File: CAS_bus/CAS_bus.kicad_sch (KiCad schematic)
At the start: 1 part, among them J5 CAS_stacking

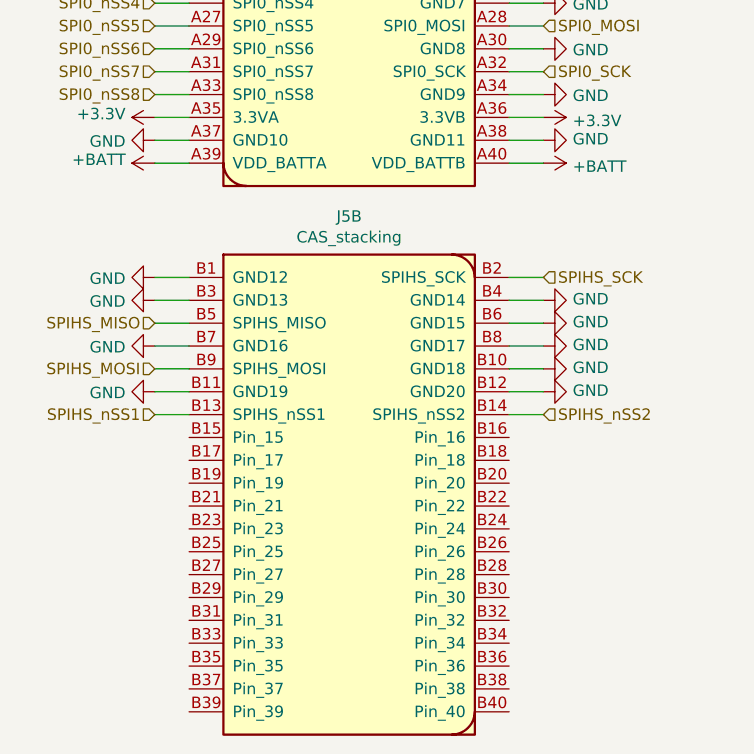
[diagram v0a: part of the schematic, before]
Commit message: Updated-cas-bus-sch
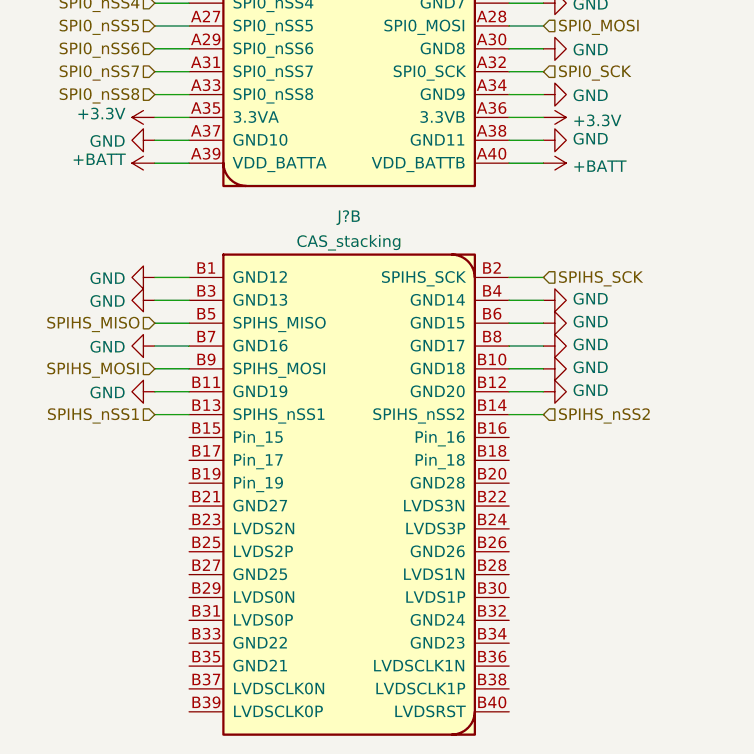
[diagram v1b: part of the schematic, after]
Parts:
- removed unit 2 of J5
- added J?: CAS_stacking, symbol star-common-lib:CAS_stacking
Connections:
- net GND: now also J?.B1 (GND12), J?.B10 (GND18), J?.B11 (GND19), J?.B12 (GND20), J?.B3 (GND13), J?.B4 (GND14), J?.B6 (GND15), J?.B7 (GND16), J?.B8 (GND17)
- net SPIHS_MISO: now also J?.B5 (SPIHS_MISO)
- net SPIHS_MOSI: now also J?.B9 (SPIHS_MOSI)
- net SPIHS_SCK: now also J?.B2 (SPIHS_SCK)
- net SPIHS_nSS1: now also J?.B13 (SPIHS_nSS1)
- net SPIHS_nSS2: now also J?.B14 (SPIHS_nSS2)
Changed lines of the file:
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@@
     (pin "1")
+  )
+  (symbol (lib_name "CAS_stacking_1") (lib_id "star-common-lib:CAS_stacking") (at 130.81 130.81 0) (unit 2)
+    (in_bom yes) (on_board yes) (fields_autoplaced)
+    (property "Reference" "J?" (id 0) (at 130.81 99.9195 0))
+    (property "Value" "CAS_stacking" (id 1) (at 130.81 102.6946 0))
+    (property "Footprint" "" (id 2) (at 133.35 106.68 0)
+      (effects (font (size 1.27 1.27)) hide)
+    )
+    (property "Datasheet" "" (id 3) (at 133.35 106.68 0)
+      (effects (font (size 1.27 1.27)) hide)
+    )
+    (pin "B1")
+    (pin "B10")
+    (pin "B11")
+    (pin "B12")
+    (pin "B13")
+    (pin "B14")
+    (pin "B15")
+    (pin "B16")
+    (pin "B17")
+    (pin "B18")
+    (pin "B19")
+    (pin "B2")
+    (pin "B20")
+    (pin "B21")
+    (pin "B22")
+    (pin "B23")
+    (pin "B24")
+    (pin "B25")
+    (pin "B26")
+    (pin "B27")
+    (pin "B28")
+    (pin "B29")
+    (pin "B3")
+    (pin "B30")
+    (pin "B31")
+    (pin "B32")
+    (pin "B33")
+    (pin "B34")
+    (pin "B35")
+    (pin "B36")
+    (pin "B37")
+    (pin "B38")
+    (pin "B39")
+    (pin "B4")
+    (pin "B40")
+    (pin "B5")
+    (pin "B6")
+    (pin "B7")
+    (pin "B8")
+    (pin "B9")
   )
   (symbol (lib_id "star-common-lib:CAS_stacking") (at 130.81 69.85 0) (unit 1)
@@
     (pin "A9")
   )
-  (symbol (lib_id "star-common-lib:CAS_stacking") (at 130.81 130.81 0) (unit 2)
-    (in_bom yes) (on_board yes)
-    (property "Reference" "J5" (id 0) (at 130.81 99.8982 0))
-    (property "Value" "CAS_stacking" (id 1) (at 130.81 102.2096 0))
-    (property "Footprint" "star-common-lib:CAS_physical" (id 2) (at 133.35 106.68 0)
-      (effects (font (size 1.27 1.27)) hide)
-    )
-    (property "Datasheet" "" (id 3) (at 133.35 106.68 0)
-      (effects (font (size 1.27 1.27)) hide)
-    )
-    (pin "B1")
-    (pin "B10")
-    (pin "B11")
-    (pin "B12")
-    (pin "B13")
-    (pin "B14")
-    (pin "B15")
-    (pin "B16")
-    (pin "B17")
-    (pin "B18")
-    (pin "B19")
-    (pin "B2")
-    (pin "B20")
-    (pin "B21")
-    (pin "B22")
-    (pin "B23")
-    (pin "B24")
-    (pin "B25")
-    (pin "B26")
-    (pin "B27")
-    (pin "B28")
-    (pin "B29")
-    (pin "B3")
-    (pin "B30")
-    (pin "B31")
-    (pin "B32")
-    (pin "B33")
-    (pin "B34")
-    (pin "B35")
-    (pin "B36")
-    (pin "B37")
-    (pin "B38")
-    (pin "B39")
-    (pin "B4")
-    (pin "B40")
-    (pin "B5")
-    (pin "B6")
-    (pin "B7")
-    (pin "B8")
-    (pin "B9")
-  )
   (sheet_instances
     (path "/" (page "1"))
@@
       (reference "J5") (unit 1) (value "CAS_stacking") (footprint "star-common-lib:CAS_physical")
     )
-    (path "/00000000-0000-0000-0000-00005f2fc6a4"
-      (reference "J5") (unit 2) (value "CAS_stacking") (footprint "star-common-lib:CAS_physical")
-    )
-  )
+    (path "/0092f24c-03a9-4895-ae75-d11a8369284a"
+      (reference "J?") (unit 2) (value "CAS_stacking") (footprint "")
+    )
+  )

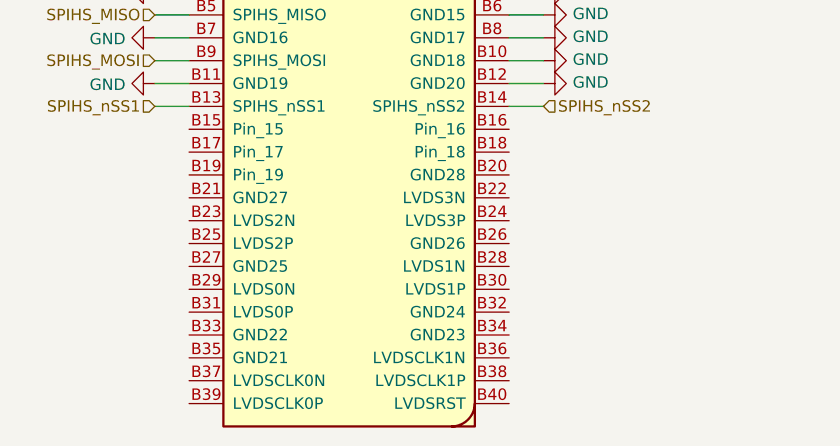
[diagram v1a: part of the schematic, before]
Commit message: Updating-heirarichical-sheet
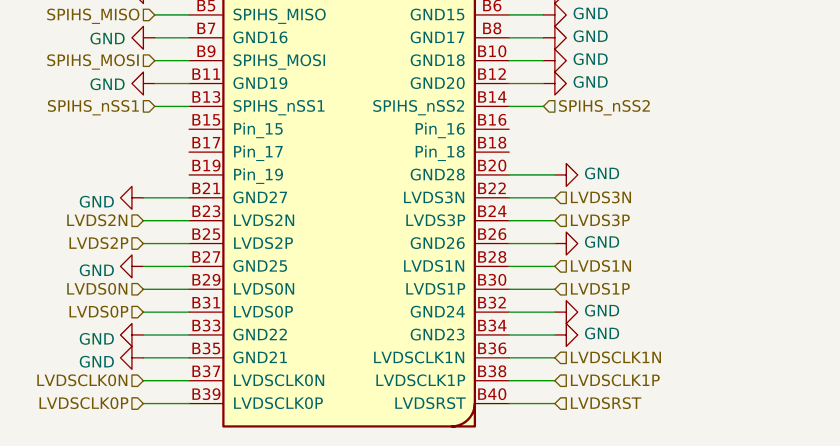
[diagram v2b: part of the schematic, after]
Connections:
- net GND: now also J?.B20 (GND28), J?.B21 (GND27), J?.B26 (GND26), J?.B27 (GND25), J?.B32 (GND24), J?.B33 (GND22), J?.B34 (GND23), J?.B35 (GND21)
- net LVDS3N: now reaches J?.B22 (LVDS3N)
- net LVDS2N: now reaches J?.B23 (LVDS2N)
- net LVDS3P: now reaches J?.B24 (LVDS3P)
- net LVDS2P: now reaches J?.B25 (LVDS2P)
- net LVDS1N: now reaches J?.B28 (LVDS1N)
- net LVDS0N: now reaches J?.B29 (LVDS0N)
- net LVDS1P: now reaches J?.B30 (LVDS1P)
- net LVDS0P: now reaches J?.B31 (LVDS0P)
- net LVDSCLK1N: now reaches J?.B36 (LVDSCLK1N)
- net LVDSCLK0N: now reaches J?.B37 (LVDSCLK0N)
- net LVDSCLK1P: now reaches J?.B38 (LVDSCLK1P)
- net LVDSCLK0P: now reaches J?.B39 (LVDSCLK0P)
- net LVDSRST: now reaches J?.B40 (LVDSRST)

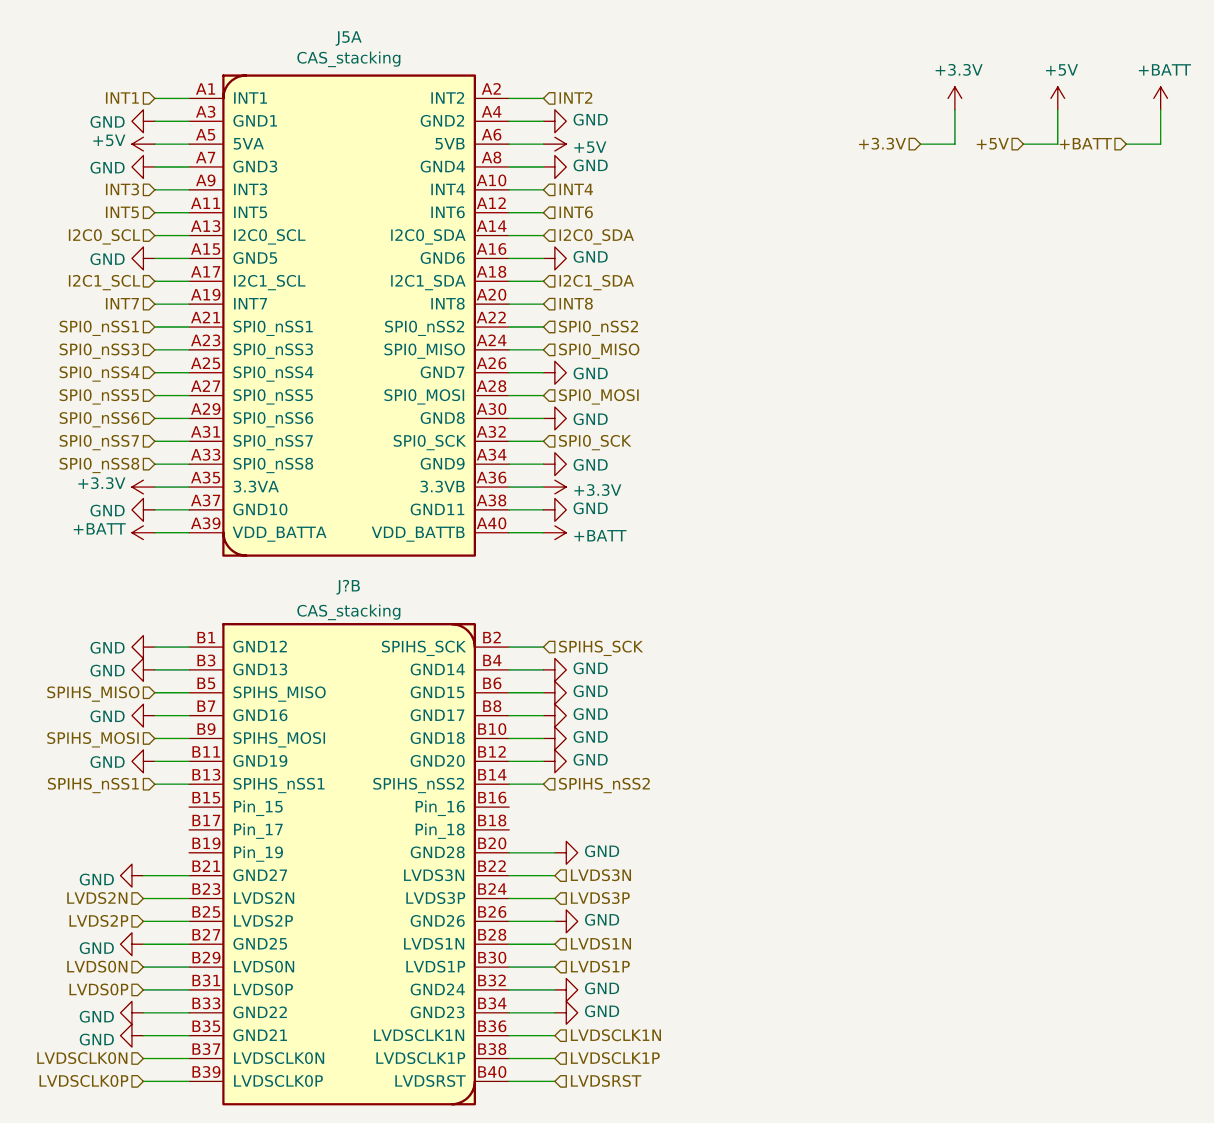
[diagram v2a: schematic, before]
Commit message: updating files to kicad 6 compatibility
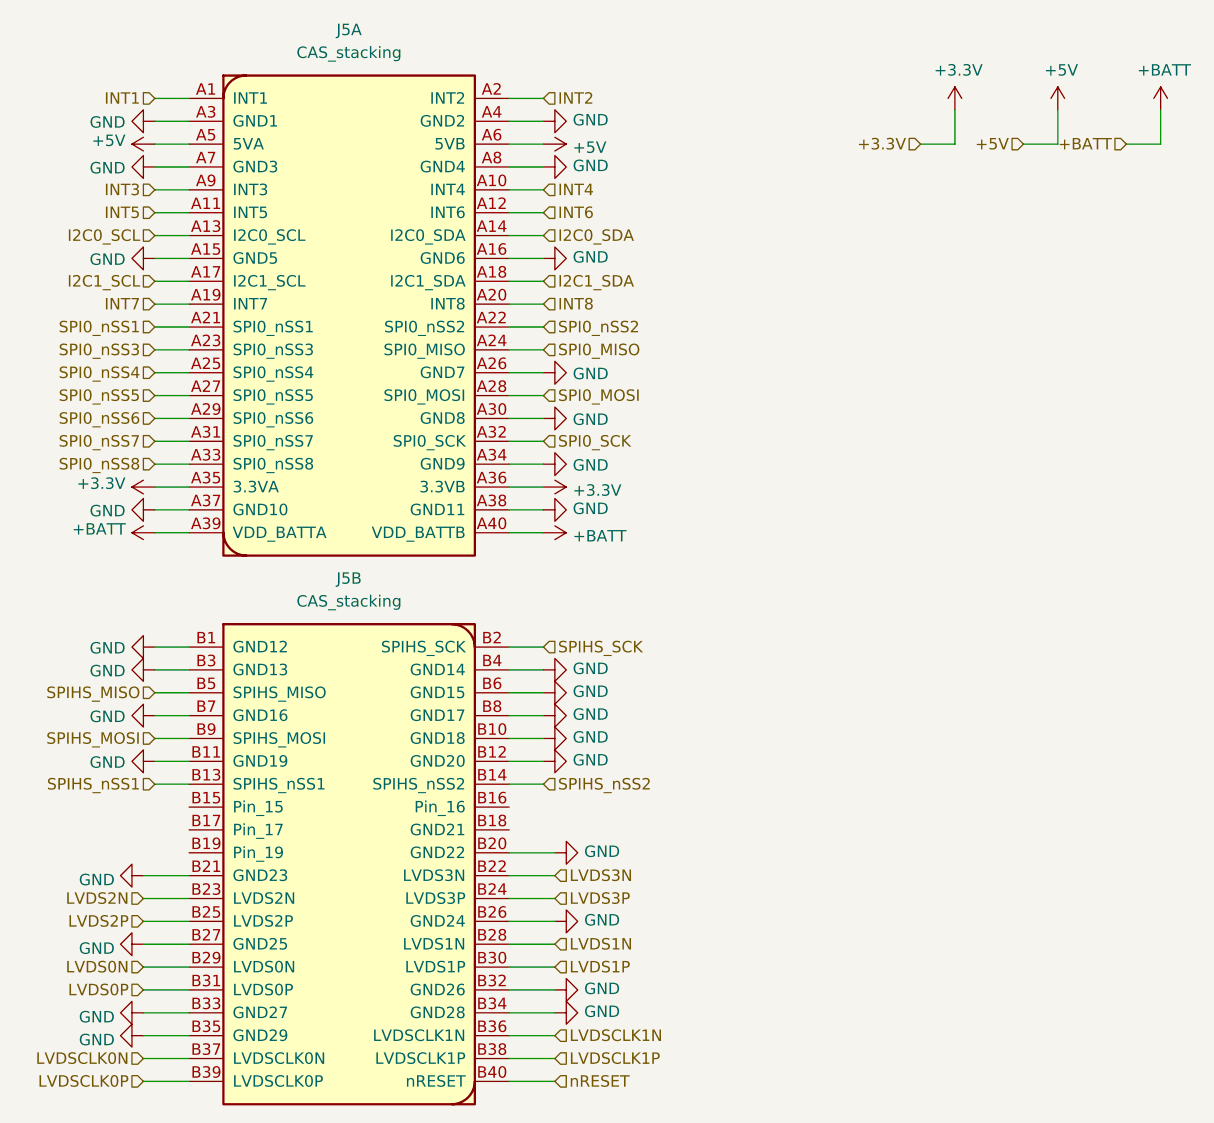
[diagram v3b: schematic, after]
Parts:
- removed J?: CAS_stacking, symbol star-common-lib:CAS_stacking
- added unit 2 of J5
- J5: footprint star-common-lib:CAS_physical -> (none)
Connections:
- net GND: now also J5.B1 (GND12), J5.B10 (GND18), J5.B11 (GND19), J5.B12 (GND20), J5.B20 (GND22), J5.B21 (GND23), J5.B26 (GND24), J5.B27 (GND25), J5.B3 (GND13), J5.B32 (GND26), J5.B33 (GND27), J5.B34 (GND28), J5.B35 (GND29), J5.B4 (GND14), J5.B6 (GND15), J5.B7 (GND16), J5.B8 (GND17)
- net LVDS0N: now also J5.B29 (LVDS0N)
- net LVDS0P: now also J5.B31 (LVDS0P)
- net LVDS1N: now also J5.B28 (LVDS1N)
- net LVDS1P: now also J5.B30 (LVDS1P)
- net LVDS2N: now also J5.B23 (LVDS2N)
- net LVDS2P: now also J5.B25 (LVDS2P)
- net LVDS3N: now also J5.B22 (LVDS3N)
- net LVDS3P: now also J5.B24 (LVDS3P)
- net LVDSCLK0N: now also J5.B37 (LVDSCLK0N)
- net LVDSCLK0P: now also J5.B39 (LVDSCLK0P)
- net LVDSCLK1N: now also J5.B36 (LVDSCLK1N)
- net LVDSCLK1P: now also J5.B38 (LVDSCLK1P)
- net SPIHS_MISO: now also J5.B5 (SPIHS_MISO)
- net SPIHS_MOSI: now also J5.B9 (SPIHS_MOSI)
- net SPIHS_SCK: now also J5.B2 (SPIHS_SCK)
- net SPIHS_nSS1: now also J5.B13 (SPIHS_nSS1)
- net SPIHS_nSS2: now also J5.B14 (SPIHS_nSS2)
- new net nRESET: J5.B40 (nRESET)

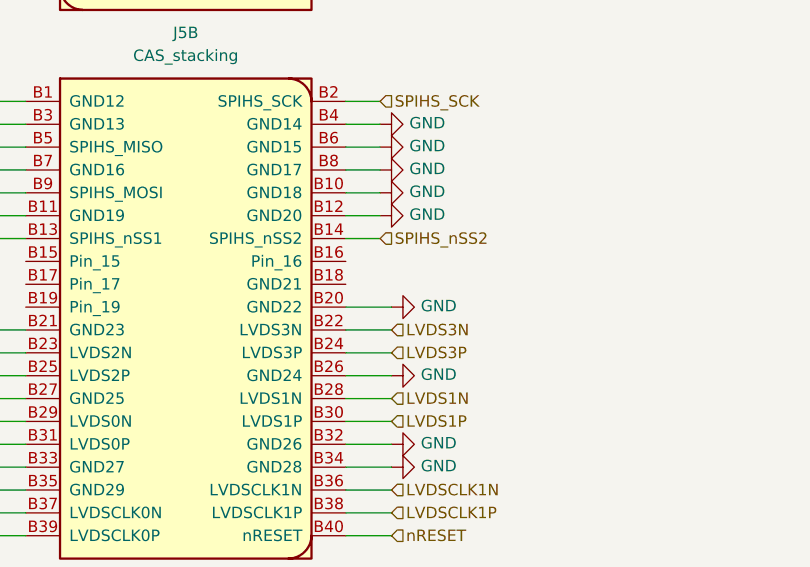
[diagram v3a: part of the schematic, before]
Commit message: add more grounding
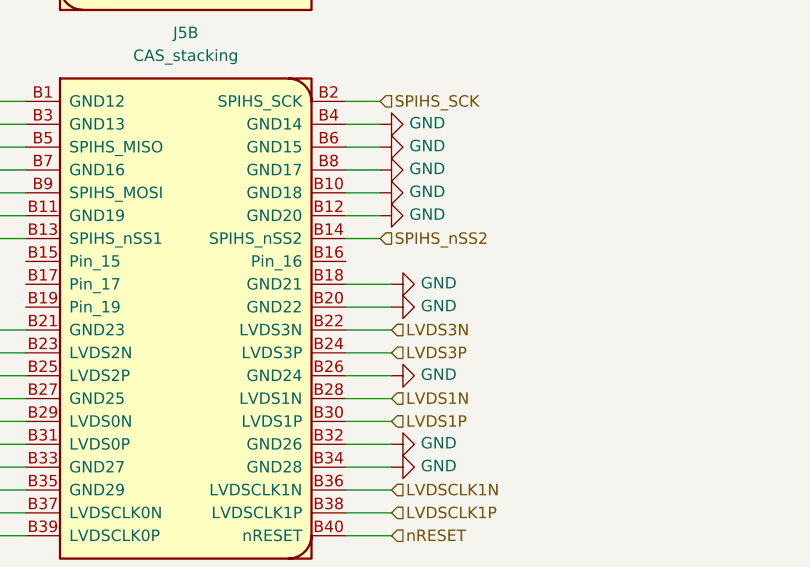
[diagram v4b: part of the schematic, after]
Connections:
- net GND: now also J5.B18 (GND21)
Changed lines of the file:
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@@
+    (stroke (width 0) (type default) (color 0 0 0 0))
+  )
+  (wire (pts (xy 148.59 127) (xy 153.67 127))
     (stroke (width 0) (type default) (color 0 0 0 0))
   )
@@
     (pin "A9")
   )
+  (symbol (lib_id "power:GND") (at 153.67 127 90) (unit 1)
+    (in_bom yes) (on_board yes)
+    (property "Reference" "#PWR?" (id 0) (at 160.02 127 0)
+      (effects (font (size 1.27 1.27)) hide)
+    )
+    (property "Value" "GND" (id 1) (at 156.9212 126.873 90)
+      (effects (font (size 1.27 1.27)) (justify right))
+    )
+    (property "Footprint" "" (id 2) (at 153.67 127 0)
+      (effects (font (size 1.27 1.27)) hide)
+    )
+    (property "Datasheet" "" (id 3) (at 153.67 127 0)
+      (effects (font (size 1.27 1.27)) hide)
+    )
+    (pin "1")
+  )
   (symbol (lib_id "power:GND") (at 153.67 129.54 90) (unit 1)
